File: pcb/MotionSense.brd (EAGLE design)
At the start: 59.4 x 59.2 mm, 18 parts

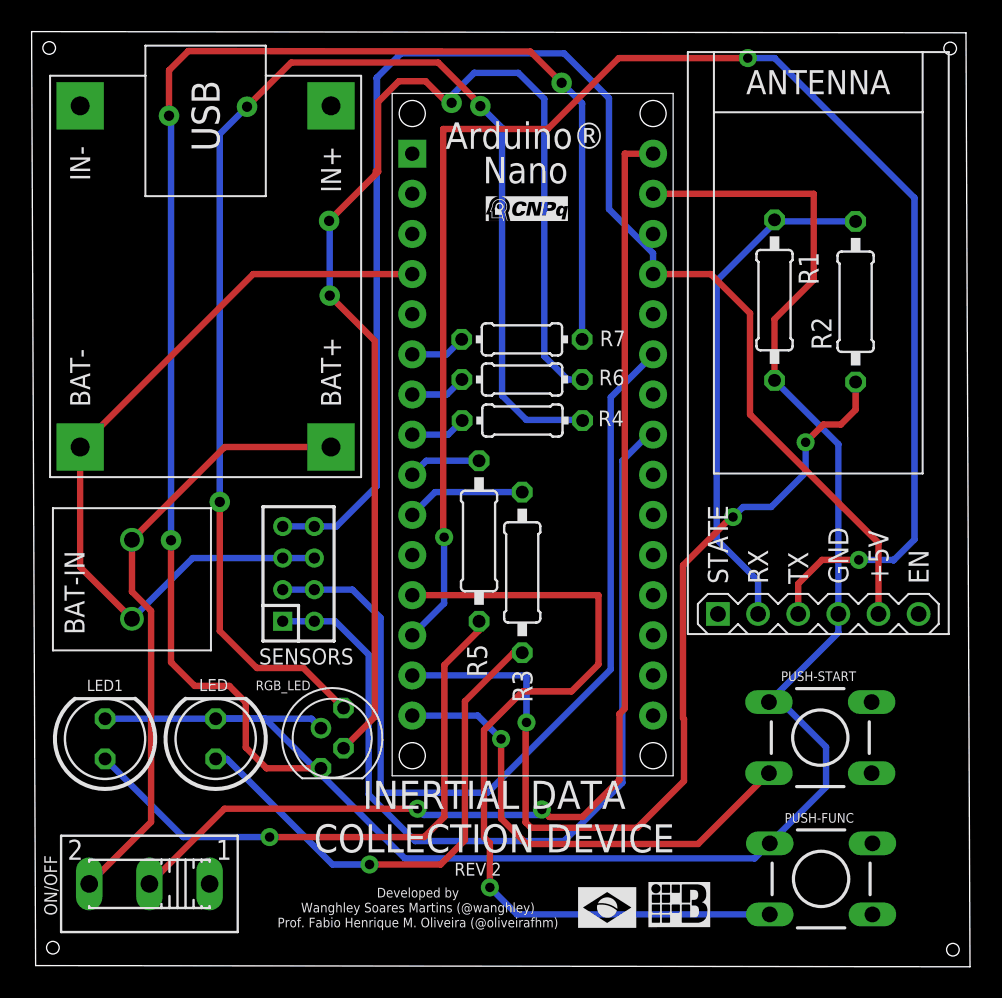
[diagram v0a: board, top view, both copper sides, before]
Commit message: [UPDATE] correction 90deg angles removing
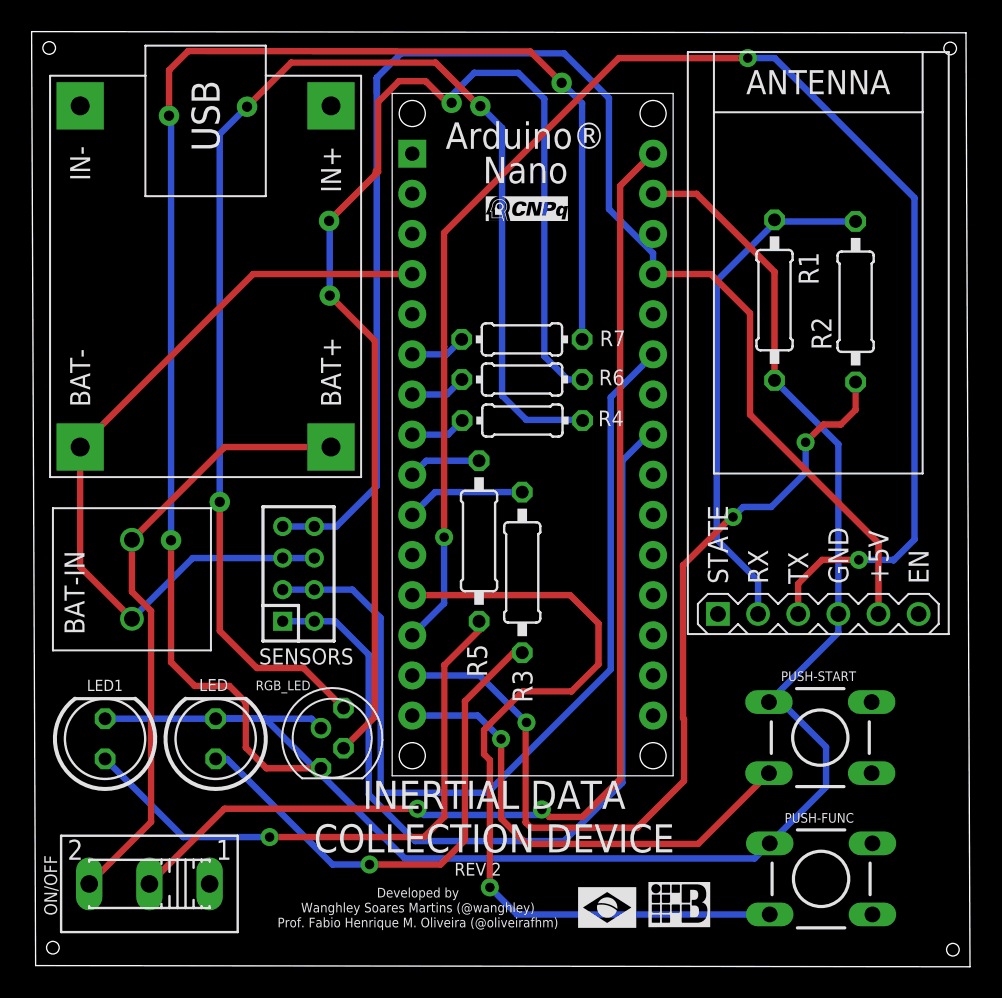
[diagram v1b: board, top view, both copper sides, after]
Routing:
- net N$4: track 112.2 -> 105.8 mm
- net N$5: track 100.3 -> 96.5 mm
- net N$3: track 59.8 -> 58.0 mm
- net N$12: track 53.7 -> 52.6 mm
- net N$11: track 75.0 -> 73.9 mm
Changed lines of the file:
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@@
 <drawing>
 <settings>
-<setting alwaysvectorfont="no"/>
+<setting alwaysvectorfont="yes"/>
 <setting verticaltext="up"/>
 </settings>
@@
 <wire x1="69.3432" y1="31.8156" x2="73.7362" y2="36.2086" width="0.4064" layer="16"/>
 <wire x1="73.7362" y1="36.2086" x2="73.7362" y2="37.3888" width="0.4064" layer="16"/>
-<wire x1="69.6976" y1="52.1716" x2="69.6976" y2="56.0451" width="0.4064" layer="1"/>
-<wire x1="72.1741" y1="58.5216" x2="72.1741" y2="63.9800625" width="0.4064" layer="1"/>
-<wire x1="72.1741" y1="63.9800625" x2="62.0115625" y2="63.9800625" width="0.4064" layer="1"/>
-<wire x1="69.6976" y1="56.0451" x2="72.1741" y2="58.5216" width="0.4064" layer="1"/>
 <wire x1="69.394" y1="22.8748" x2="72.958959375" y2="26.439759375" width="0.4064" layer="16"/>
 <wire x1="72.958959375" y1="26.439759375" x2="72.958959375" y2="28.971240625" width="0.4064" layer="16"/>
@@
 <wire x1="34.3306375" y1="30.7594" x2="40.39804375" y2="30.7594" width="0.4064" layer="16"/>
 <wire x1="40.39804375" y1="30.7594" x2="40.992403125" y2="30.165040625" width="0.4064" layer="16"/>
+<wire x1="69.6976" y1="52.1716" x2="69.6976" y2="59.039759375" width="0.4064" layer="1"/>
+<wire x1="64.757296875" y1="63.9800625" x2="62.0115625" y2="63.9800625" width="0.4064" layer="1"/>
+<wire x1="69.6976" y1="59.039759375" x2="64.757296875" y2="63.9800625" width="0.4064" layer="1"/>
 </signal>
 <signal name="N$5">
@@
 <contactref element="ARDUINO-NANO" pad="J1.13"/>
 <wire x1="71.1962" y1="37.3888" x2="71.1962" y2="39.303959375" width="0.4064" layer="1"/>
-<wire x1="48.7299" y1="68.0821625" x2="48.7299" y2="42.308778125" width="0.4064" layer="1"/>
 <wire x1="48.7299" y1="42.308778125" x2="48.78831875" y2="42.250359375" width="0.4064" layer="1"/>
 <via x="48.78831875" y="42.250359375" extent="1-16" drill="0.6" diameter="1.15"/>
@@
 <wire x1="78.55711875" y1="63.718440625" x2="69.707759375" y2="72.5678" width="0.4064" layer="16"/>
 <wire x1="68.005959375" y1="72.5678" x2="59.83731875" y2="72.5678" width="0.4064" layer="1"/>
-<wire x1="59.83731875" y1="72.5678" x2="55.35168125" y2="68.0821625" width="0.4064" layer="1"/>
-<wire x1="55.35168125" y1="68.0821625" x2="48.7299" y2="68.0821625" width="0.4064" layer="1"/>
+<wire x1="48.78324375" y1="54.30455" x2="48.78831875" y2="54.299475" width="0.4064" layer="1"/>
+<wire x1="48.78831875" y1="54.299475" x2="48.78831875" y2="42.250359375" width="0.4064" layer="1"/>
+<wire x1="48.78324375" y1="61.513725" x2="48.78324375" y2="54.30455" width="0.4064" layer="1"/>
+<wire x1="59.83731875" y1="72.5678" x2="48.78324375" y2="61.513725" width="0.4064" layer="1"/>
 </signal>
 <signal name="N$3">
@@
 <wire x1="53.94451875" y1="30.4698375" x2="54.0004" y2="30.52571875" width="0.4064" layer="1"/>
 <via x="54.0004" y="30.52571875" extent="1-16" drill="0.6" diameter="1.15"/>
-<wire x1="54.0004" y1="30.52571875" x2="54.0004" y2="33.5000625" width="0.4064" layer="16"/>
-<wire x1="54.0004" y1="33.5000625" x2="46.7715625" y2="33.5000625" width="0.4064" layer="16"/>
 <wire x1="63.9699" y1="30.73004375" x2="63.9699" y2="26.819859375" width="0.4064" layer="1"/>
 <wire x1="54.28488125" y1="23.860759375" x2="53.94451875" y2="24.201121875" width="0.4064" layer="1"/>
@@
 <wire x1="73.89368125" y1="49.3776" x2="74.8284" y2="50.31231875" width="0.4064" layer="1"/>
 <wire x1="74.8284" y1="50.31231875" x2="74.8284" y2="52.07" width="0.4064" layer="1"/>
+<wire x1="46.7715625" y1="33.5000625" x2="51.02605625" y2="33.5000625" width="0.4064" layer="16"/>
+<wire x1="51.02605625" y1="33.5000625" x2="54.0004" y2="30.52571875" width="0.4064" layer="16"/>
 </signal>
 <signal name="N$6">
@@
 <contactref element="ON/OFF" pad="2"/>
 <contactref element="ARDUINO-NANO" pad="J2.1"/>
-<wire x1="62.0115625" y1="66.5200625" x2="60.220859375" y2="66.5200625" width="0.4064" layer="1"/>
-<wire x1="60.220859375" y1="31.400603125" x2="59.8805" y2="31.06024375" width="0.4064" layer="1"/>
-<wire x1="59.8805" y1="26.8859" x2="59.8805" y2="31.06024375" width="0.4064" layer="1"/>
-<wire x1="60.220859375" y1="31.400603125" x2="60.220859375" y2="66.5200625" width="0.4064" layer="1"/>
-<wire x1="57.5371375" y1="24.5425375" x2="55.45085625" y2="24.5425375" width="0.4064" layer="1"/>
+<wire x1="55.45085625" y1="24.5425375" x2="57.5371375" y2="24.5425375" width="0.4064" layer="1"/>
 <wire x1="54.97671875" y1="25.016675" x2="55.45085625" y2="24.5425375" width="0.4064" layer="1"/>
-<wire x1="57.5371375" y1="24.5425375" x2="59.8805" y2="26.8859" width="0.4064" layer="1"/>
 <wire x1="34.89451875" y1="25.06471875" x2="47.106840625" y2="25.06471875" width="0.4064" layer="1"/>
 <via x="47.106840625" y="25.06471875" extent="1-16" drill="0.6" diameter="1.15"/>
@@
 <via x="54.97671875" y="25.016675" extent="1-16" drill="0.6" diameter="1.15"/>
 <wire x1="30.1371" y1="20.3073" x2="34.89451875" y2="25.06471875" width="0.4064" layer="1"/>
+<wire x1="59.928759375" y1="26.934159375" x2="59.928759375" y2="64.48551875" width="0.4064" layer="1"/>
+<wire x1="59.928759375" y1="64.48551875" x2="61.963303125" y2="66.5200625" width="0.4064" layer="1"/>
+<wire x1="61.963303125" y1="66.5200625" x2="62.0115625" y2="66.5200625" width="0.4064" layer="1"/>
+<wire x1="57.5371375" y1="24.5425375" x2="59.928759375" y2="26.934159375" width="0.4064" layer="1"/>
 </signal>
 <signal name="N$2">
@@
 <wire x1="53.3954375" y1="18.3748" x2="51.68391875" y2="20.08631875" width="0.4064" layer="16"/>
 <via x="51.68391875" y="20.08631875" extent="1-16" drill="0.6" diameter="1.15"/>
-<wire x1="51.68391875" y1="20.08631875" x2="51.68391875" y2="22.89048125" width="0.4064" layer="1"/>
-<wire x1="51.68391875" y1="22.89048125" x2="51.31308125" y2="23.26131875" width="0.4064" layer="1"/>
-<wire x1="51.31308125" y1="23.26131875" x2="51.31308125" y2="30.05328125" width="0.4064" layer="1"/>
-<wire x1="53.75148125" y1="32.49168125" x2="56.85028125" y2="32.49168125" width="0.4064" layer="1"/>
-<wire x1="56.85028125" y1="32.49168125" x2="58.55208125" y2="34.19348125" width="0.4064" layer="1"/>
-<wire x1="58.55208125" y1="34.19348125" x2="58.55208125" y2="38.5800625" width="0.4064" layer="1"/>
-<wire x1="58.55208125" y1="38.5800625" x2="46.7715625" y2="38.5800625" width="0.4064" layer="1"/>
+<wire x1="51.31308125" y1="28.514040625" x2="51.31308125" y2="30.05328125" width="0.4064" layer="1"/>
+<wire x1="56.85028125" y1="32.49168125" x2="53.75148125" y2="32.49168125" width="0.4064" layer="1"/>
 <wire x1="51.31308125" y1="30.05328125" x2="53.75148125" y2="32.49168125" width="0.4064" layer="1"/>
+<wire x1="46.7715625" y1="38.5800625" x2="56.76645625" y2="38.5800625" width="0.4064" layer="1"/>
+<wire x1="56.76645625" y1="38.5800625" x2="58.557159375" y2="36.789359375" width="0.4064" layer="1"/>
+<wire x1="58.557159375" y1="36.789359375" x2="58.557159375" y2="34.198559375" width="0.4064" layer="1"/>
+<wire x1="58.557159375" y1="34.198559375" x2="56.85028125" y2="32.49168125" width="0.4064" layer="1"/>
+<wire x1="51.68391875" y1="28.143203125" x2="51.31308125" y2="28.514040625" width="0.4064" layer="1"/>
+<wire x1="51.68391875" y1="20.08631875" x2="51.68391875" y2="28.143203125" width="0.4064" layer="1"/>
 </signal>
 <signal name="AREF">
@@
 <wire x1="57.4929" y1="49.8221" x2="57.4929" y2="49.819559375" width="0.4064" layer="16"/>
 <wire x1="36.316921875" y1="69.489321875" x2="39.11091875" y2="72.28331875" width="0.4064" layer="1"/>
-<wire x1="39.11091875" y1="72.28331875" x2="48.4124" y2="72.28331875" width="0.4064" layer="1"/>
-<wire x1="48.4124" y1="72.28331875" x2="51.0794" y2="69.61631875" width="0.4064" layer="1"/>
-<wire x1="51.0794" y1="69.61631875" x2="51.0794" y2="69.529959375" width="0.4064" layer="1"/>
+<wire x1="39.11091875" y1="72.28331875" x2="48.249840625" y2="72.28331875" width="0.4064" layer="1"/>
+<wire x1="48.249840625" y1="72.28331875" x2="50.8609625" y2="69.672196875" width="0.4064" layer="1"/>
+<wire x1="50.9371625" y1="69.672196875" x2="50.8609625" y2="69.672196875" width="0.4064" layer="1"/>
+<wire x1="50.9371625" y1="69.672196875" x2="51.0794" y2="69.529959375" width="0.4064" layer="1"/>
 <via x="51.0794" y="69.529959375" extent="1-16" drill="0.65" diameter="1.3"/>
 <wire x1="51.0794" y1="69.529959375" x2="52.45608125" y2="68.153278125" width="0.4064" layer="16"/>

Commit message: [UPDATE] change RGB ports to right PWM
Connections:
- net N$13: now also ARDUINO-NANO.J1.11; no longer ARDUINO-NANO.J1.9
- net N$21: no longer ARDUINO-NANO.J1.7
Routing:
- net N$13: track 4.59 -> 9.53 mm
- net N$21: track 3.53 -> 0.00 mm
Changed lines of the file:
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@@
 <drawing>
 <settings>
-<setting alwaysvectorfont="yes"/>
+<setting alwaysvectorfont="no"/>
 <setting verticaltext="up"/>
 </settings>
@@
 <element name="LED" library="led" library_urn="urn:adsk.eagle:library:259" package="LED5MM" package3d_urn="urn:adsk.eagle:package:15799/2" value="power indicator" x="34.3306375" y="29.4894" smashed="yes" rot="R90">
 <attribute name="NAME" x="35.123115625" y="33.274" size="0.762" layer="25" ratio="10" rot="R180"/>
-<attribute name="VALUE" x="30.7238375" y="26.5684" size="0.6096" layer="27" ratio="10" rot="R90"/>
+<attribute name="VALUE" x="36.9316" y="25.948640625" size="0.6096" layer="27" ratio="10" rot="R180"/>
 </element>
 <element name="PUSH-START" library="switch-tact" package="DTS-6" value="DTS-6" x="72.5932" y="29.5656" smashed="yes">
@@
 <element name="LED1" library="led" library_urn="urn:adsk.eagle:library:259" package="LED5MM" package3d_urn="urn:adsk.eagle:package:15799/2" value="collection indicator" x="27.3304" y="29.4894" smashed="yes" rot="R90">
 <attribute name="NAME" x="28.458159375" y="33.225740625" size="0.7112" layer="25" ratio="10" rot="R180"/>
-<attribute name="VALUE" x="31.5722" y="26.3398" size="0.6096" layer="27" ratio="10" rot="R90"/>
+<attribute name="VALUE" x="23.85568125" y="26.289" size="0.6096" layer="27" ratio="10" rot="R90"/>
 </element>
 <element name="R5" library="eagle-ltspice" library_urn="urn:adsk.eagle:library:217" package="0207/10" package3d_urn="urn:adsk.eagle:package:13275/1" value="330R" x="50.99811875" y="42.00651875" smashed="yes" rot="R90">
@@
 <wire x1="47.5234" y1="23.27148125" x2="48.803559375" y2="24.551640625" width="0.4064" layer="1"/>
 </signal>
-<signal name="N$13">
-<contactref element="R5" pad="2"/>
-<contactref element="ARDUINO-NANO" pad="J1.9"/>
-<wire x1="50.99811875" y1="47.08651875" x2="47.65801875" y2="47.08651875" width="0.4064" layer="16"/>
-<wire x1="47.65801875" y1="47.08651875" x2="46.7715625" y2="46.2000625" width="0.4064" layer="16"/>
-</signal>
 <signal name="N$12">
 <contactref element="PUSH-FUNC" pad="3"/>
@@
 <wire x1="49.039784375" y1="48.7400625" x2="46.7715625" y2="48.7400625" width="0.4064" layer="16"/>
 </signal>
-<signal name="N$21">
-<contactref element="R6" pad="1"/>
-<contactref element="ARDUINO-NANO" pad="J1.7"/>
-<wire x1="49.910996875" y1="52.227478125" x2="48.96358125" y2="51.2800625" width="0.4064" layer="16"/>
-<wire x1="48.96358125" y1="51.2800625" x2="46.7715625" y2="51.2800625" width="0.4064" layer="16"/>
-</signal>
 <signal name="N$22">
 <contactref element="R7" pad="1"/>
@@
 <wire x1="57.52084375" y1="69.70775625" x2="57.52084375" y2="54.767478125" width="0.4064" layer="16"/>
 </signal>
+<signal name="N$13">
+<contactref element="R5" pad="2"/>
+<contactref element="ARDUINO-NANO" pad="J1.11"/>
+<wire x1="46.7715625" y1="41.1200625" x2="49.801784375" y2="41.1200625" width="0.3048" layer="1"/>
+<wire x1="49.801784375" y1="41.1200625" x2="51.043840625" y2="42.36211875" width="0.3048" layer="1"/>
+<wire x1="51.043840625" y1="42.36211875" x2="51.043840625" y2="47.040796875" width="0.3048" layer="1"/>
+<wire x1="51.043840625" y1="47.040796875" x2="50.99811875" y2="47.08651875" width="0.3048" layer="1"/>
+</signal>
+<signal name="N$21">
+<contactref element="R6" pad="1"/>
+</signal>
 </signals>
